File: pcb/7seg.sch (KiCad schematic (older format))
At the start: 28 parts, among them Q10 2SC1815, Q11 2SC1815, Q12 2SC1815, Q13 2SC1815, Q14 2SC1815, Q9 2SC1815, U7 7seg-2digit-ca, U8 7seg-2digit-ca, U9 7seg-2digit-ca

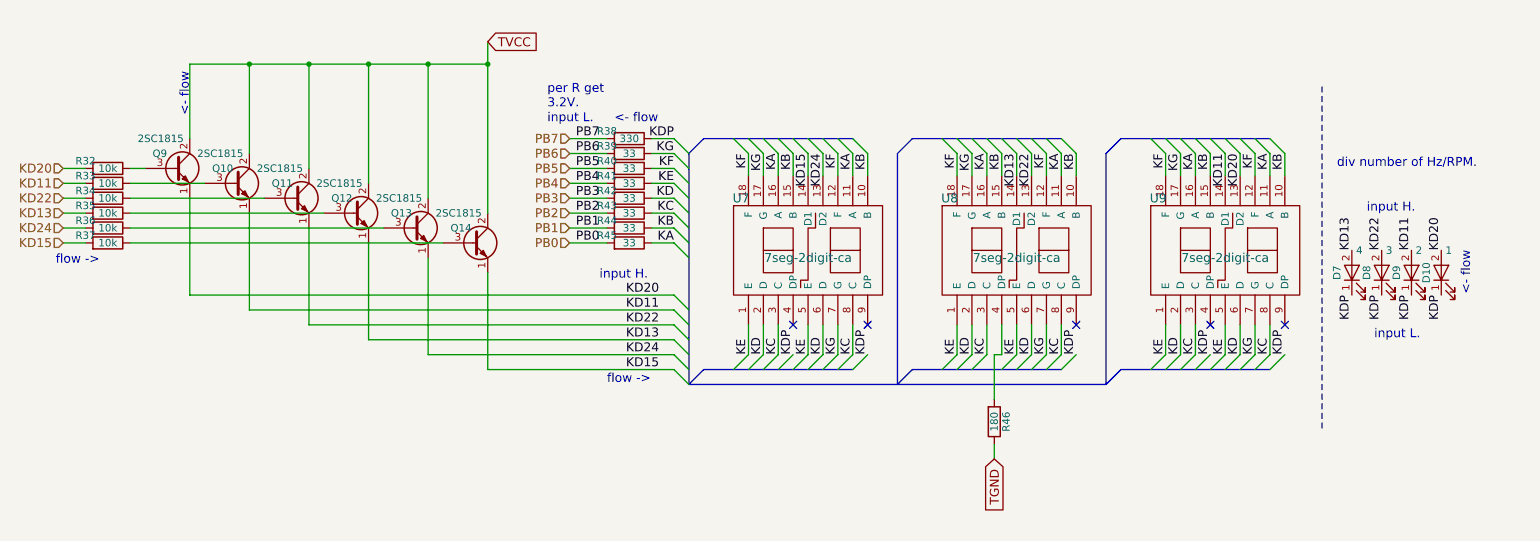
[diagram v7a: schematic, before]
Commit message: 基本的に入出力に関する，7SEG, LED, PUSH-BUTTONを2階に配置する。
2階-1階の直登戦術でいこうと思う。
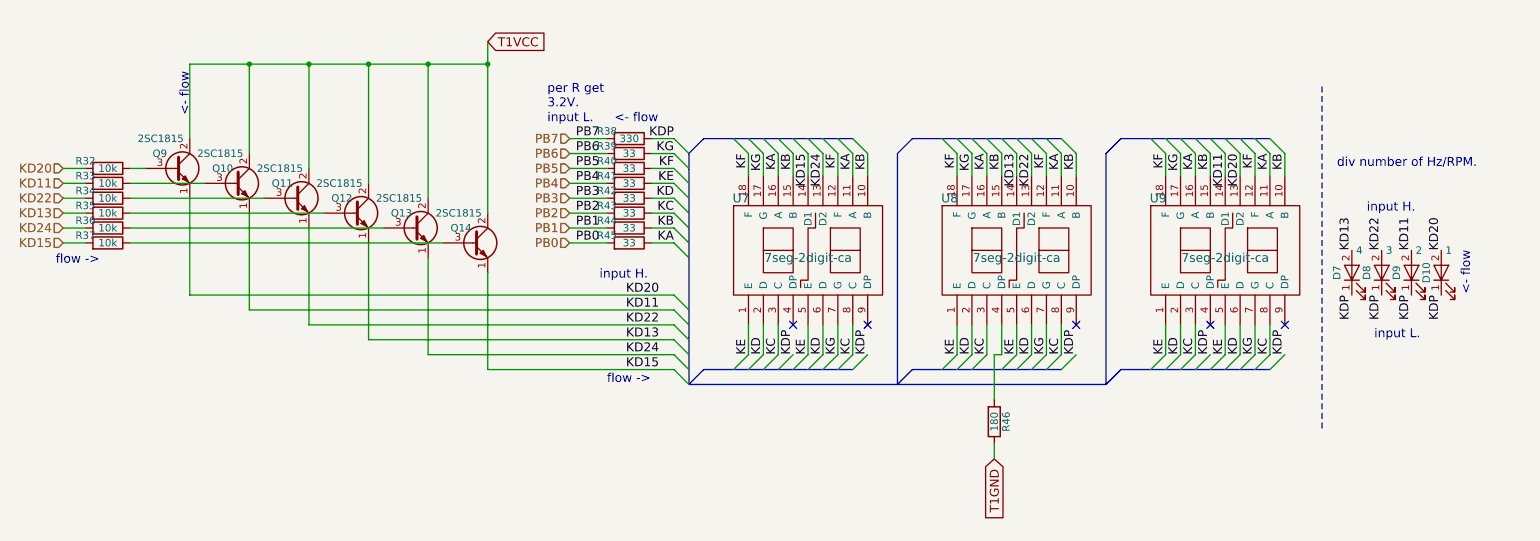
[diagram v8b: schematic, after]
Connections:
- net TGND renamed T1GND
- net TVCC renamed T1VCC
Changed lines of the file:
@@
 $EndComp
 Text GLabel 7100 4600 3    60   Input ~ 0
-TGND
+T1GND
 $Comp
 L 2SC1815 Q9
@@
 <- flow
 Text GLabel 3700 1800 2    60   Input ~ 0
-TVCC
+T1VCC
 Wire Wire Line
 	3300 3900 4950 3900
